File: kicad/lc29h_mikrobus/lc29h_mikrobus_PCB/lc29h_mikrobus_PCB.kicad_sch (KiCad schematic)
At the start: 46 parts, among them IC1 MIKROE-924, IC2 DS28E36BQ+U, IC3 74LVC1G3157GV,125, J1 Conn_Coaxial, J2 Conn_01x03_Pin, Q1 MMBT2222A, Q2 DMP3013SFV, Q4 BSS123L, Q5 BSS123L, Q6 MMBT2222A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

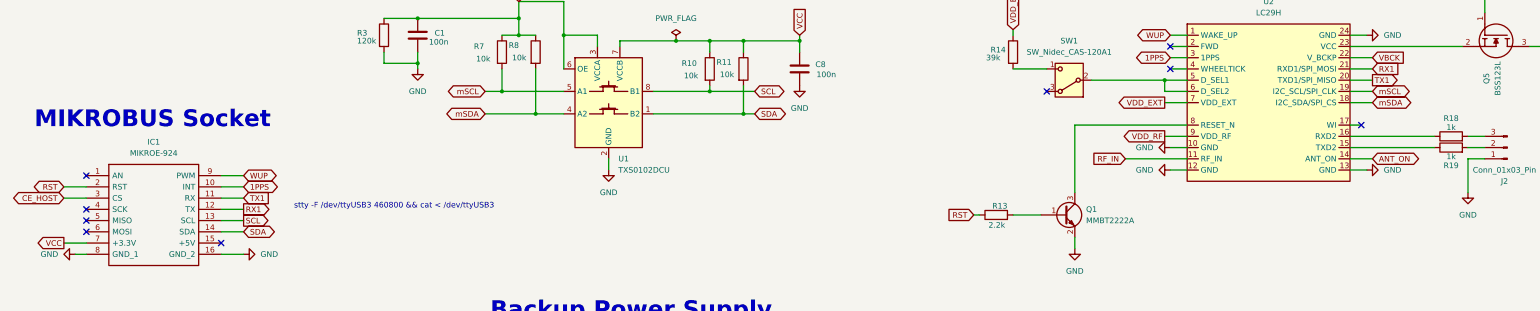
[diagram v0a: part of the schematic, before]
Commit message: pull up resistors and remove silkscreen warnings
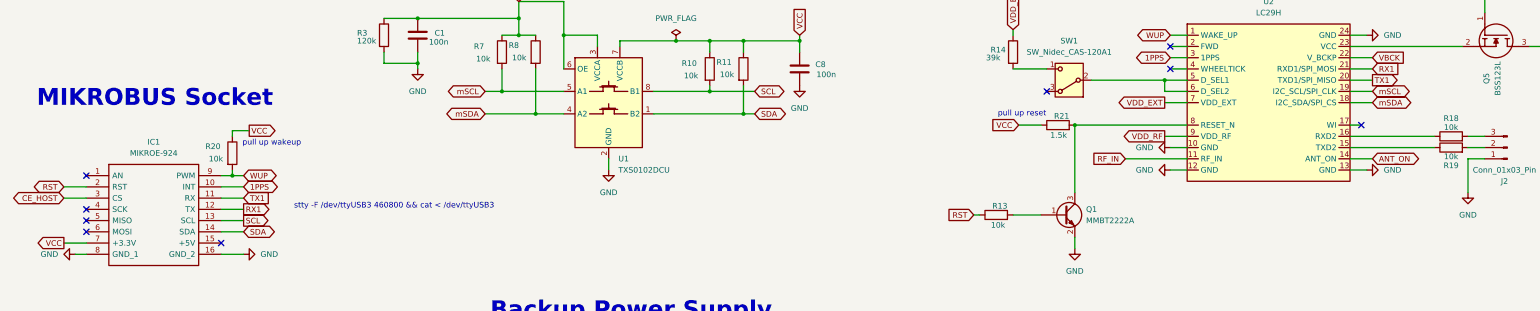
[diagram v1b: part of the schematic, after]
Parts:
- added R20: 10k, Resistor_SMD:R_0805_2012Metric_Pad1.20x1.40mm_HandSolder, symbol Device:R
- added R21: 1.5k, Resistor_SMD:R_0805_2012Metric_Pad1.20x1.40mm_HandSolder, symbol Device:R
- R13: value 2.2k -> 10k
- R18, R19: value 1k -> 10k
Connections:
- net VCC: now also R20.1, R21.1
- net WUP: now also R20.2
- net at Q1.3 (C), U2.8 (RESET_N): now also R21.2
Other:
- note added: "pull up reset"
- note added: "pull up wakeup"
